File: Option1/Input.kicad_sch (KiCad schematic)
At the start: 1 part, among them J501 Conn_01x08_Pin

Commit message: SPI Flash hinzugefügt, IN/Outputs vereinheitlicht, USB Flash Möglichkeit hinzugefügt, Display fehtl noch
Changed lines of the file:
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@@
 (kicad_sch
-	(version 20231120)
+	(version 20250114)
 	(generator "eeschema")
-	(generator_version "8.0")
+	(generator_version "9.0")
 	(paper "A4")
 	(title_block
@@
 		(comment 2 "Bachelorarbiet")
 		(comment 3 "Sebastian Hampl")
+	)
+	(text_box "Pinheader als Platzhalter für Stecker"
+		(exclude_from_sim no)
+		(at 13.97 59.69 0)
+		(size 16.256 10.668)
+		(margins 1.143 1.143 1.143 1.143)
+		(stroke
+			(width 0.381)
+			(type default)
+			(color 251 0 0 1)
+		)
+		(fill
+			(type none)
+		)
+		(effects
+			(font
+				(size 1.27 1.27)
+				(color 255 0 0 1)
+			)
+			(justify left top)
+		)
 	)
 	(wire
@@
 		)
 	)
-	(text_box "Pinheader als Platzhalter für Stecker"
-		(exclude_from_sim no)
-		(at 13.97 59.69 0)
-		(size 16.256 10.668)
-		(stroke
-			(width 0.381)
-			(type default)
-			(color 251 0 0 1)
-		)
-		(fill
-			(type none)
-		)
-		(effects
-			(font
-				(size 1.27 1.27)
-				(color 255 0 0 1)
-			)
-			(justify left top)
-		)
-	)

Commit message: Erste issues eingearbeitet
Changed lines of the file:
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@@
+		)
+	)
+	(label "48V_IN"
+		(at 41.91 21.59 0)
+		(effects
+			(font
+				(size 1.27 1.27)
+			)
+			(justify left bottom)
+		)
+	)
+	(label "GND"
+		(at 41.91 24.13 0)
+		(effects
+			(font
+				(size 1.27 1.27)
+			)
+			(justify left bottom)
 		)
 	)

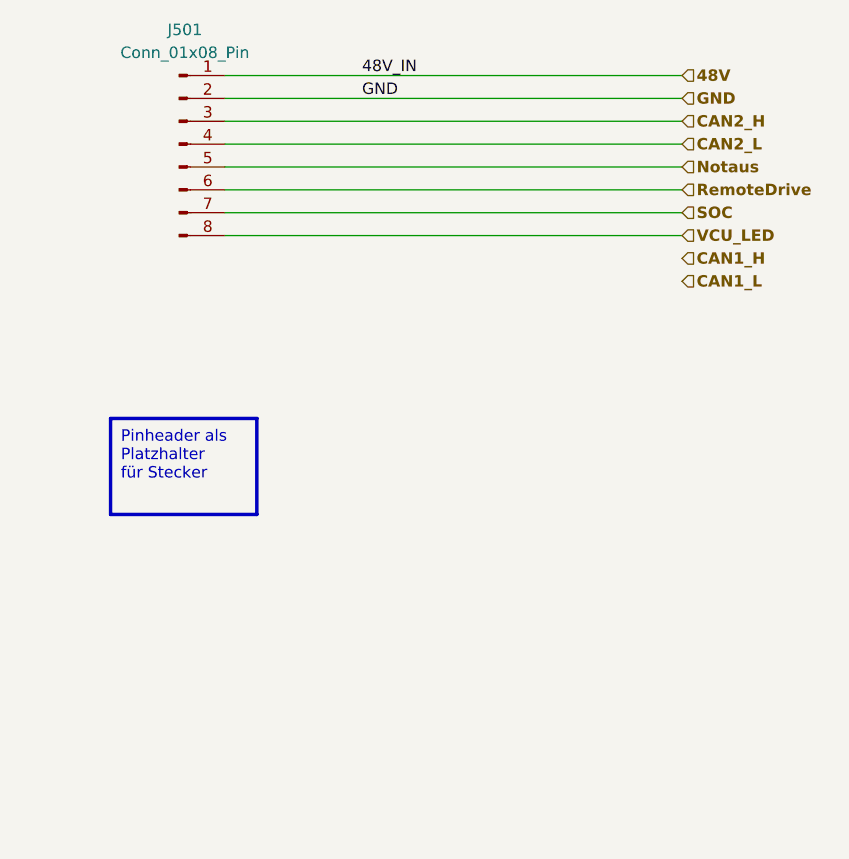
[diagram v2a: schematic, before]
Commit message: Alte Stecker zum litzen verschrauben auf Platine vorgesehn, 14 Pin Stecker zum Stecken fehlt, RFID und LED abklären
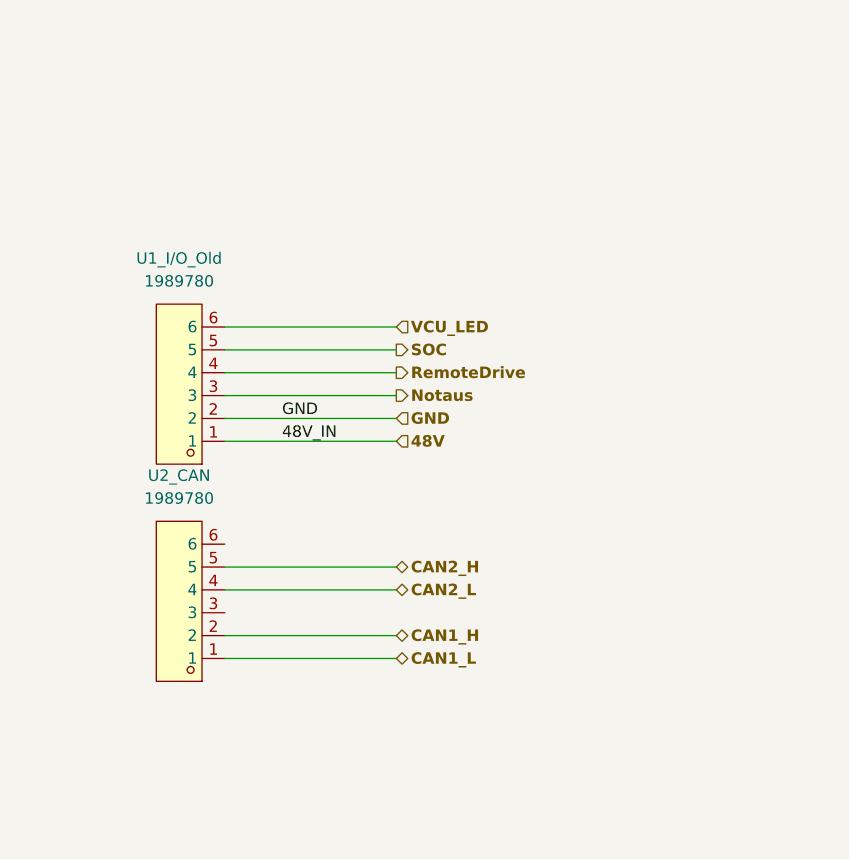
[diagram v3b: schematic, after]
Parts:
- removed J501: Conn_01x08_Pin, symbol Connector:Conn_01x08_Pin
- added U1_I/O_Old, U2_CAN: 1989780, easyeda2kicad:CONN-TH_6P-P2.50_1989780, symbol EasyEda2KiCad:1989780
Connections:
- net 48V: now also U1_I/O_Old.1
- net CAN1_H: now also U2_CAN.2
- net CAN1_L: now also U2_CAN.1
- net CAN2_H: now also U2_CAN.5
- net CAN2_L: now also U2_CAN.4
- net GND: now also U1_I/O_Old.2
- net Notaus: now also U1_I/O_Old.3
- net RemoteDrive: now also U1_I/O_Old.4
- net SOC: now also U1_I/O_Old.5
- net VCU_LED: now also U1_I/O_Old.6

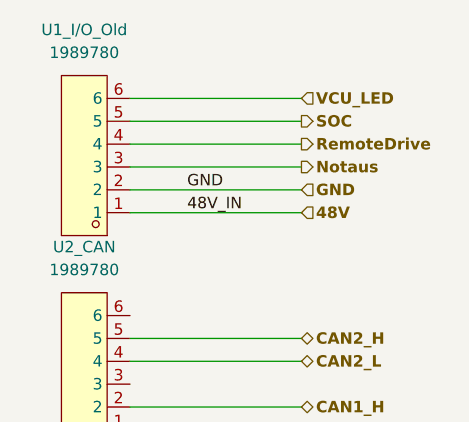
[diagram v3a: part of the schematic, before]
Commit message: USB Schaltung angepasst, Transistoren korrigiert, Stecker ausgetauscht, Dioden hinzugefügt
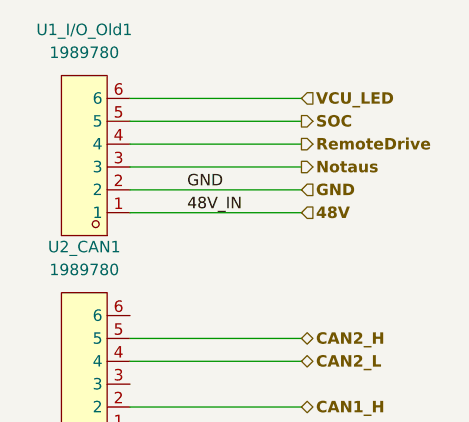
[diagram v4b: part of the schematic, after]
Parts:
- renumbered U1_I/O_Old to U1_I/O_Old1, U2_CAN to U2_CAN1
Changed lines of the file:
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@@
 		(dnp no)
 		(fields_autoplaced yes)
-		(property "Reference" "U1_I/O_Old"
+		(property "Reference" "U1_I/O_Old1"
 			(at 21.59 41.91 0)
 			(effects
@@
 			(project ""
 				(path "/b9e5f262-9648-4b79-bdd1-af888b822329/f9f0c67f-dd50-4740-b345-6512cc3de02a"
-					(reference "U1_I/O_Old")
+					(reference "U1_I/O_Old1")
 					(unit 1)
 				)
@@
 		(dnp no)
 		(fields_autoplaced yes)
-		(property "Reference" "U2_CAN"
+		(property "Reference" "U2_CAN1"
 			(at 21.59 66.04 0)
 			(effects
@@
 			(project "Option1"
 				(path "/b9e5f262-9648-4b79-bdd1-af888b822329/f9f0c67f-dd50-4740-b345-6512cc3de02a"
-					(reference "U2_CAN")
+					(reference "U2_CAN1")
 					(unit 1)
 				)

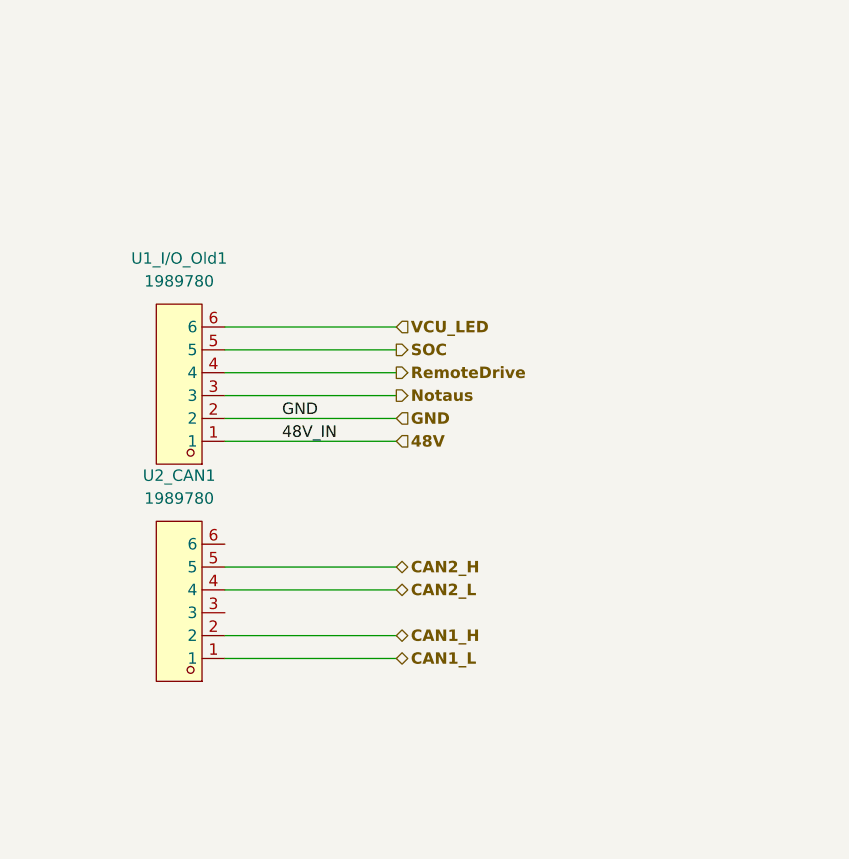
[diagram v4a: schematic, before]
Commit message: Layout für Powersupply, CAN und Stecker hinzugefügt
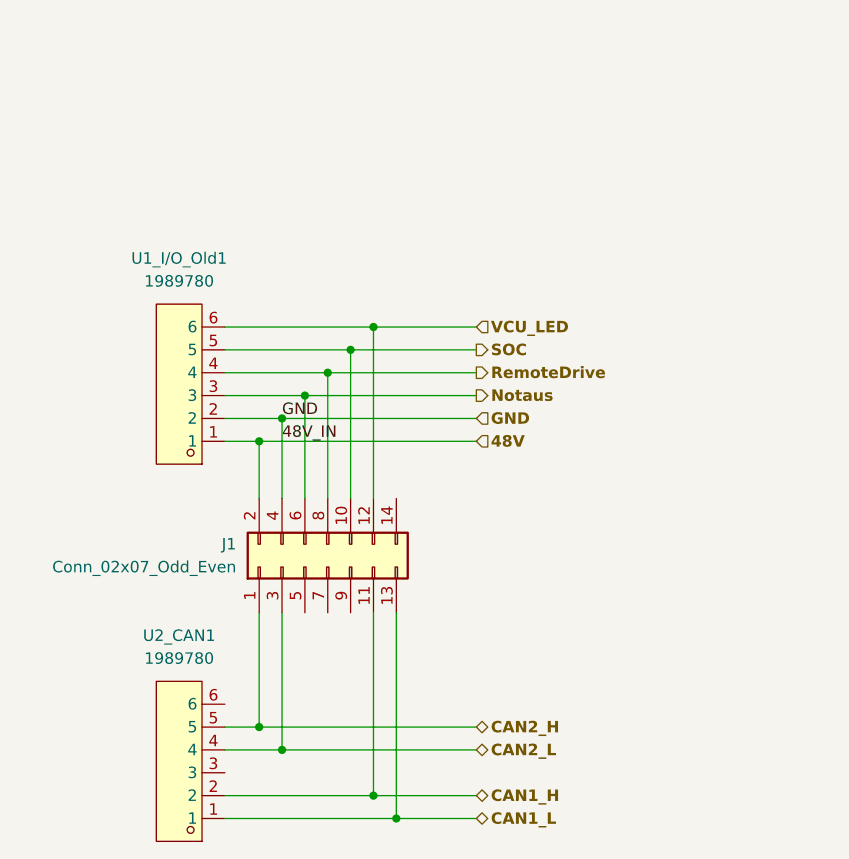
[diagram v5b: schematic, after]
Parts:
- added J1: Conn_02x07_Odd_Even, Connector_PinHeader_2.54mm:PinHeader_2x07_P2.54mm_Vertical, symbol Connector_Generic:Conn_02x07_Odd_Even
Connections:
- net GND is gone; now on net 48V: U1_I/O_Old1.2
- net 48V: now also J1.2 (Pin_2), J1.4 (Pin_4)
- net CAN1_H: now also J1.11 (Pin_11)
- net CAN1_L: now also J1.13 (Pin_13)
- net CAN2_H: now also J1.1 (Pin_1)
- net CAN2_L: now also J1.3 (Pin_3)
- net Notaus: now also J1.6 (Pin_6)
- net RemoteDrive: now also J1.8 (Pin_8)
- net SOC: now also J1.10 (Pin_10)
- net VCU_LED: now also J1.12 (Pin_12)
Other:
- moved on the sheet: U2_CAN1

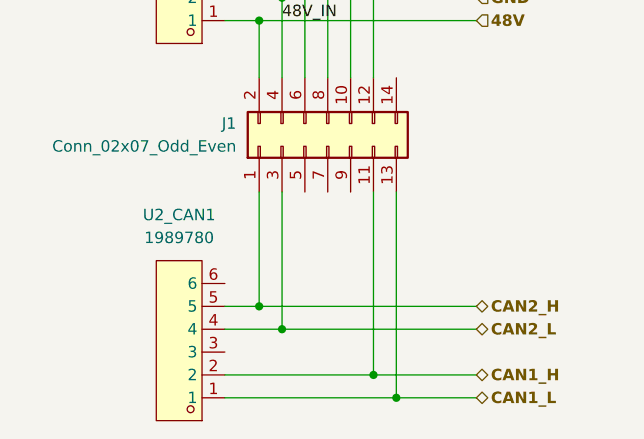
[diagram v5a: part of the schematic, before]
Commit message: MCT und SPI zu Layout hinzugefügt
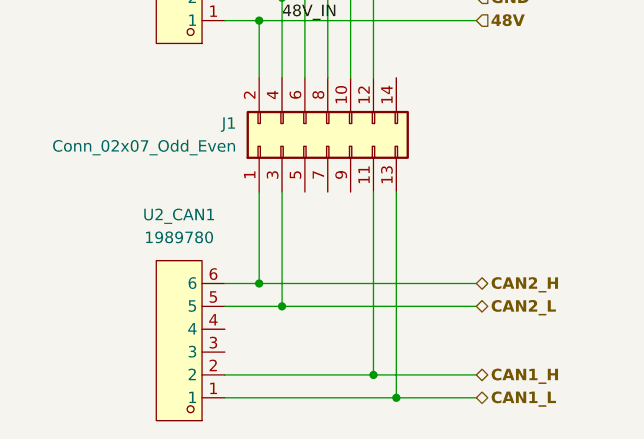
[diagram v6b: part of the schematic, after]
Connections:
- net CAN2_H: now also U2_CAN1.6; no longer U2_CAN1.5
- net CAN2_L: now also U2_CAN1.5; no longer U2_CAN1.4
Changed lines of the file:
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@@
 	)
 	(junction
-		(at 30.48 93.98)
+		(at 33.02 93.98)
 		(diameter 0)
 		(color 0 0 0 0)
@@
 	)
 	(junction
+		(at 30.48 91.44)
+		(diameter 0)
+		(color 0 0 0 0)
+	)
+	(junction
 		(at 43.18 49.53)
 		(diameter 0)
@@
 	)
 	(junction
-		(at 33.02 96.52)
+		(at 33.02 59.69)
+		(diameter 0)
+		(color 0 0 0 0)
+	)
+	(junction
+		(at 35.56 57.15)
 		(diameter 0)
 		(color 0 0 0 0)
@@
 		(color 0 0 0 0)
 	)
-	(junction
-		(at 33.02 59.69)
-		(diameter 0)
-		(color 0 0 0 0)
-	)
-	(junction
-		(at 35.56 57.15)
-		(diameter 0)
-		(color 0 0 0 0)
-	)
 	(wire
 		(pts
@@
 	(wire
 		(pts
+			(xy 26.67 93.98) (xy 33.02 93.98)
+		)
+		(stroke
+			(width 0)
+			(type default)
+		)
+	)
+	(wire
+		(pts
 			(xy 43.18 81.28) (xy 43.18 101.6)
 		)
@@
 	(wire
 		(pts
-			(xy 30.48 81.28) (xy 30.48 93.98)
-		)
-		(stroke
-			(width 0)
-			(type default)
-		)
-	)
-	(wire
-		(pts
-			(xy 26.67 93.98) (xy 30.48 93.98)
+			(xy 30.48 81.28) (xy 30.48 91.44)
 		)
 		(stroke
@@
 	(wire
 		(pts
-			(xy 26.67 96.52) (xy 33.02 96.52)
-		)
-		(stroke
-			(width 0)
-			(type default)
-		)
-	)
-	(wire
-		(pts
 			(xy 33.02 59.69) (xy 54.61 59.69)
 		)
@@
 	(wire
 		(pts
+			(xy 26.67 101.6) (xy 43.18 101.6)
+		)
+		(stroke
+			(width 0)
+			(type default)
+		)
+	)
+	(wire
+		(pts
 			(xy 33.02 59.69) (xy 33.02 68.58)
 		)
@@
 	(wire
 		(pts
+			(xy 54.61 101.6) (xy 43.18 101.6)
+		)
+		(stroke
+			(width 0)
+			(type default)
+		)
+	)
+	(wire
+		(pts
+			(xy 33.02 93.98) (xy 54.61 93.98)
+		)
+		(stroke
+			(width 0)
+			(type default)
+		)
+	)
+	(wire
+		(pts
+			(xy 26.67 91.44) (xy 30.48 91.44)
+		)
+		(stroke
+			(width 0)
+			(type default)
+		)
+	)
+	(wire
+		(pts
+			(xy 33.02 81.28) (xy 33.02 93.98)
+		)
+		(stroke
+			(width 0)
+			(type default)
+		)
+	)
+	(wire
+		(pts
+			(xy 30.48 91.44) (xy 54.61 91.44)
+		)
+		(stroke
+			(width 0)
+			(type default)
+		)
+	)
+	(wire
+		(pts
+			(xy 26.67 49.53) (xy 43.18 49.53)
+		)
+		(stroke
+			(width 0)
+			(type default)
+		)
+	)
+	(wire
+		(pts
+			(xy 38.1 54.61) (xy 54.61 54.61)
+		)
+		(stroke
+			(width 0)
+			(type default)
+		)
+	)
+	(wire
+		(pts
+			(xy 35.56 57.15) (xy 35.56 68.58)
+		)
+		(stroke
+			(width 0)
+			(type default)
+		)
+	)
+	(wire
+		(pts
+			(xy 43.18 49.53) (xy 54.61 49.53)
+		)
+		(stroke
+			(width 0)
+			(type default)
+		)
+	)
+	(wire
+		(pts
+			(xy 30.48 62.23) (xy 30.48 68.58)
+		)
+		(stroke
+			(width 0)
+			(type default)
+		)
+	)
+	(wire
+		(pts
 			(xy 26.67 104.14) (xy 45.72 104.14)
-		)
-		(stroke
-			(width 0)
-			(type default)
-		)
-	)
-	(wire
-		(pts
-			(xy 54.61 101.6) (xy 43.18 101.6)
-		)
-		(stroke
-			(width 0)
-			(type default)
-		)
-	)
-	(wire
-		(pts
-			(xy 33.02 96.52) (xy 54.61 96.52)
-		)
-		(stroke
-			(width 0)
-			(type default)
-		)
-	)
-	(wire
-		(pts
-			(xy 43.18 101.6) (xy 26.67 101.6)
-		)
-		(stroke
-			(width 0)
-			(type default)
-		)
-	)
-	(wire
-		(pts
-			(xy 33.02 81.28) (xy 33.02 96.52)
-		)
-		(stroke
-			(width 0)
-			(type default)
-		)
-	)
-	(wire
-		(pts
-			(xy 30.48 93.98) (xy 54.61 93.98)
-		)
-		(stroke
-			(width 0)
-			(type default)
-		)
-	)
-	(wire
-		(pts
-			(xy 26.67 49.53) (xy 43.18 49.53)
-		)
-		(stroke
-			(width 0)
-			(type default)
-		)
-	)
-	(wire
-		(pts
-			(xy 38.1 54.61) (xy 54.61 54.61)
-		)
-		(stroke
-			(width 0)
-			(type default)
-		)
-	)
-	(wire
-		(pts
-			(xy 35.56 57.15) (xy 35.56 68.58)
-		)
-		(stroke
-			(width 0)
-			(type default)
-		)
-	)
-	(wire
-		(pts
-			(xy 43.18 49.53) (xy 54.61 49.53)
-		)
-		(stroke
-			(width 0)
-			(type default)
-		)
-	)
-	(wire
-		(pts
-			(xy 30.48 62.23) (xy 30.48 68.58)
 		)
 		(stroke
@@
 	(hierarchical_label "CAN2_L"
 		(shape bidirectional)
-		(at 54.61 96.52 0)
+		(at 54.61 93.98 0)
 		(effects
 			(font
@@
 	(hierarchical_label "CAN2_H"
 		(shape bidirectional)
-		(at 54.61 93.98 0)
-		(effects
-			(font
+		(at 54.61 91.44 0)
+		(effects
+			(font
